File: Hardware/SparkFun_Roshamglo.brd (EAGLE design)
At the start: 35.6 x 72.4 mm, 48 parts, among them IC1 ATTINY84A, J1 R_Ext, J2 USBPCB, Q1 600mA/40V, U1 IR-Receiver, U3 AP2112K-3.3V

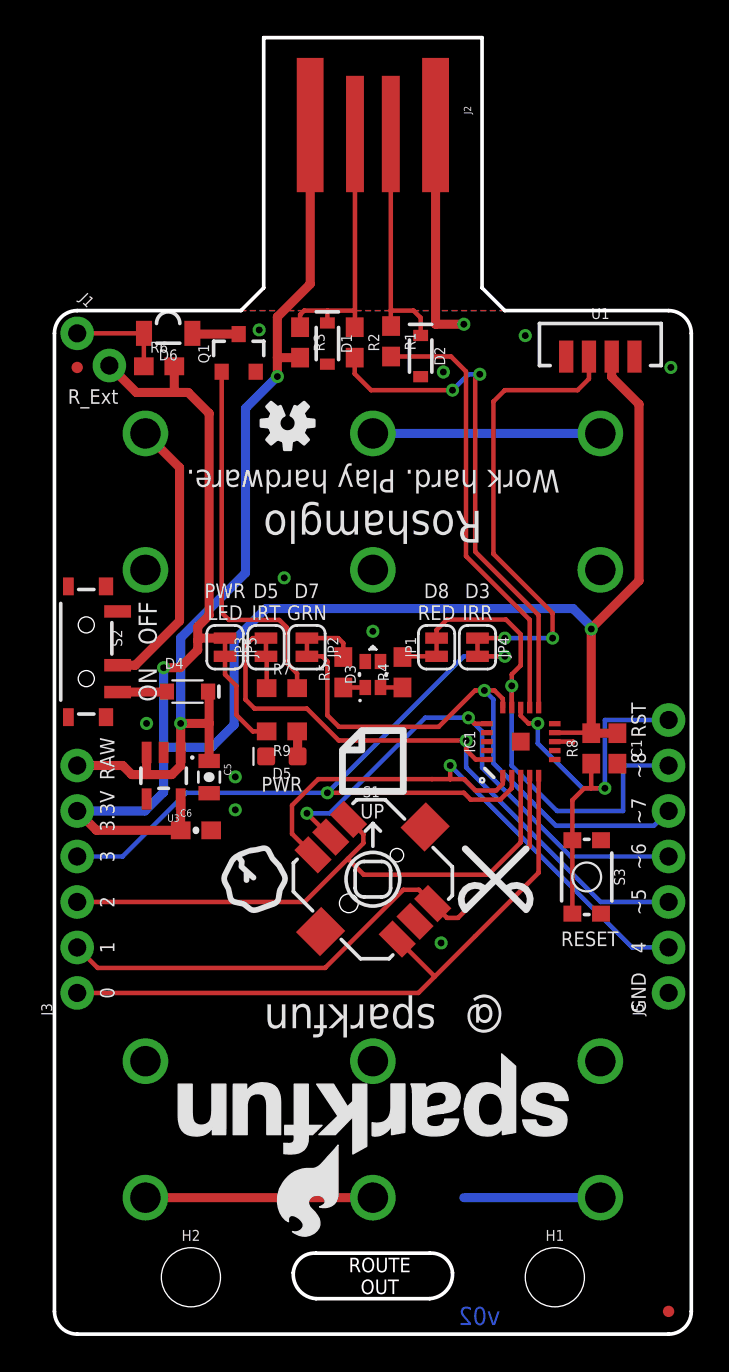
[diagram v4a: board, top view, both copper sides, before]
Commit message: Minor fixes
Added ordering instructions to bottom of board
Removed right angles in traces
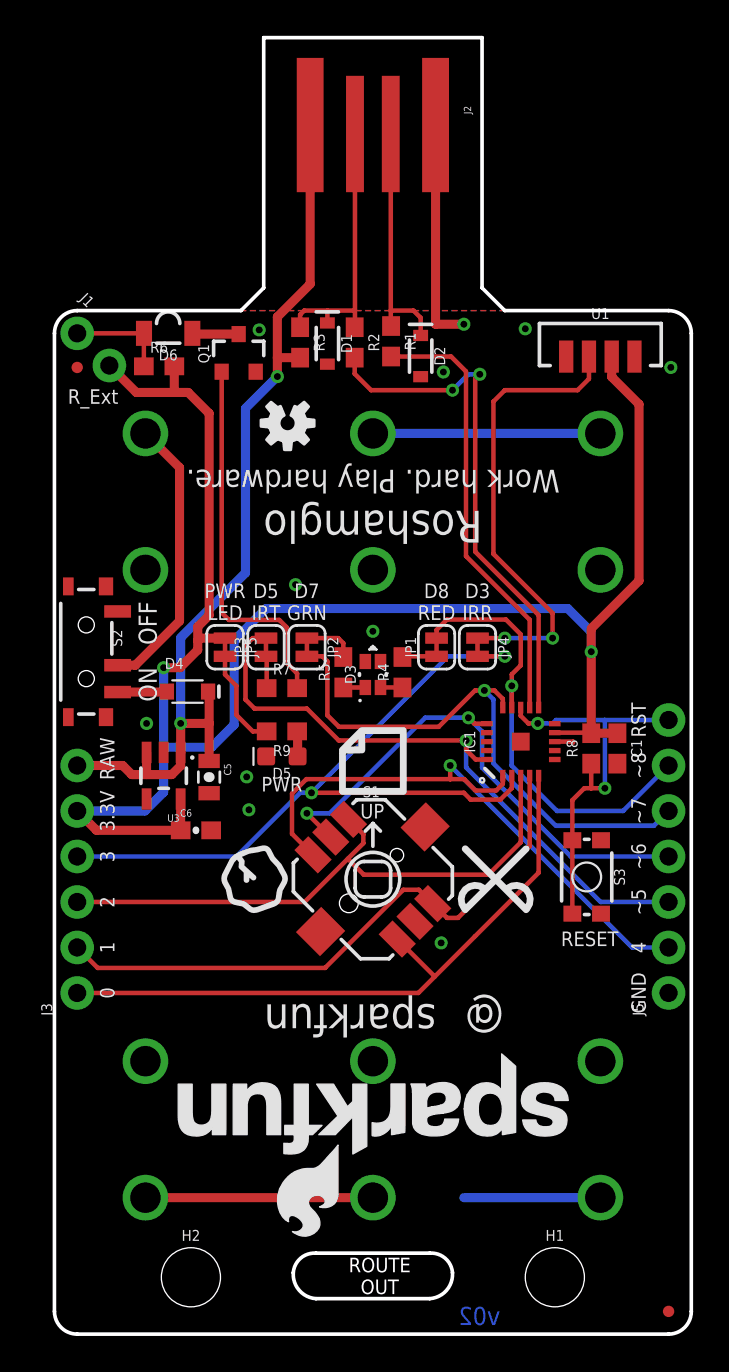
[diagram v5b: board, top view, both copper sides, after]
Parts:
- added U$5: SPECIAL_INSTRUCTIONS-ORDERING, SparkFun-Aesthetics:ORDERING_INSTRUCTIONS
- moved U$4 0.25 mm to (17.8, 67.3)
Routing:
- net !RESET: track 24.7 -> 22.6 mm
- net 8: track 26.8 -> 25.4 mm
- net 3.3V: track 102.5 -> 103.6 mm
- net 3: track 41.4 -> 42.3 mm
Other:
- board text added: "PCB Thickness: 0.078 inch"
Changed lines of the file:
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@@
 <layer number="45" name="Holes" color="7" fill="1" visible="no" active="yes"/>
 <layer number="46" name="Milling" color="3" fill="1" visible="no" active="yes"/>
-<layer number="47" name="Measures" color="7" fill="1" visible="no" active="yes"/>
+<layer number="47" name="Measures" color="7" fill="1" visible="yes" active="yes"/>
 <layer number="51" name="tDocu" color="6" fill="1" visible="yes" active="yes"/>
 <layer number="52" name="bDocu" color="7" fill="1" visible="no" active="yes"/>
@@
 <text x="18.161" y="2.2352" size="0.8128" layer="20" font="vector" ratio="15" align="bottom-center">ROUTE
 OUT</text>
-<text x="17.78" y="55.626" size="1.4224" layer="22" font="vector" ratio="15" rot="SMR180" align="bottom-center">Hack me! sfe.io/roshamglo</text>
+<text x="17.78" y="55.626" size="1.27" layer="22" font="vector" ratio="15" rot="SMR180" align="bottom-center">Hack me! sfe.io/roshamglo</text>
 <text x="17.78" y="48.26" size="1.27" layer="21" font="vector" ratio="15" rot="SR180" align="bottom-center">Work hard. Play hardware.</text>
 <text x="16.51" y="18.415" size="1.778" layer="21" font="vector" ratio="15" rot="SR180" align="bottom-center">sparkfun</text>
-<polygon width="0.0254" layer="22">
-<vertex x="12.1666" y="71.374"/>
-<vertex x="11.7348" y="72.136"/>
-<vertex x="23.8252" y="72.136"/>
-<vertex x="23.3934" y="71.374"/>
-</polygon>
 <wire x1="14.605" y1="4.5212" x2="20.955" y2="4.5212" width="0.2032" layer="20"/>
 <wire x1="20.955" y1="4.5212" x2="22.225" y2="3.429" width="0.2032" layer="20" curve="-90"/>
@@
 LED</text>
 <text x="24.003" y="18.542" size="1.778" layer="21" ratio="30" rot="SR180" align="bottom-center">@</text>
+<text x="-34.29" y="-35.56" size="1.778" layer="51" font="vector" ratio="15" align="center-left">PCB Thickness: 0.078 inch</text>
 </plain>
 <attributes>
@@
 <element name="H1" library="SparkFun-Hardware" package="STAND-OFF" value="STAND-OFF" x="27.94" y="3.175"/>
 <element name="H2" library="SparkFun-Hardware" package="STAND-OFF" value="STAND-OFF" x="7.62" y="3.175"/>
-<element name="U$4" library="Roshamglo" package="ROSHAMGLO_LOGO_0.4" value="" x="17.78" y="67.056" rot="MR180"/>
+<element name="U$4" library="Roshamglo" package="ROSHAMGLO_LOGO_0.4" value="" x="17.78" y="67.31" rot="MR180"/>
 <element name="S3" library="SparkFun-Switches" package="TACTILE_SWITCH_SMD_4.6X2.8MM" value="" x="29.718" y="25.527" rot="R270">
 <attribute name="PROD_ID" value="SWCH-13065" x="29.718" y="25.527" size="1.778" layer="27" font="vector" ratio="15" rot="R270" display="off"/>
@@
 <attribute name="PROD_ID" value="CONN-08437" x="1.27" y="19.05" size="0.8128" layer="27" ratio="30" rot="R90" display="off"/>
 </element>
+<element name="U$5" library="SparkFun-Aesthetics" package="ORDERING_INSTRUCTIONS" value="SPECIAL_INSTRUCTIONS-ORDERING" x="-36.83" y="-21.59"/>
 </elements>
 <signals>
@@
 <wire x1="7.046" y1="29.8784" x2="7.046" y2="28.1339" width="0.508" layer="1"/>
 <wire x1="7.046" y1="28.1339" x2="7.0494" y2="28.1305" width="0.508" layer="1"/>
-<via x="29.972" y="39.37" extent="1-16" drill="0.381"/>
+<via x="29.972" y="38.1" extent="1-16" drill="0.381"/>
 <wire x1="32.639" y1="51.921528125" x2="32.639" y2="42.06523125" width="0.508" layer="1"/>
 <wire x1="31.115" y1="54.58" x2="31.115" y2="53.445528125" width="0.508" layer="1"/>
@@
 <wire x1="29.972" y1="33.5835" x2="29.972" y2="33.5525" width="0.254" layer="1"/>
 <via x="6.096" y="37.211" extent="1-16" drill="0.381"/>
-<wire x1="11.811" y1="40.513" x2="28.956" y2="40.513" width="0.508" layer="16"/>
-<wire x1="28.956" y1="40.513" x2="29.972" y2="39.497" width="0.508" layer="16"/>
-<wire x1="29.972" y1="39.497" x2="29.972" y2="39.37" width="0.508" layer="16"/>
+<wire x1="11.811" y1="40.513" x2="28.66445625" y2="40.513" width="0.508" layer="16"/>
+<wire x1="28.66445625" y1="40.513" x2="29.972" y2="39.20545625" width="0.508" layer="16"/>
+<wire x1="29.972" y1="39.20545625" x2="29.972" y2="38.1" width="0.508" layer="16"/>
 <wire x1="32.639" y1="42.06523125" x2="29.972" y2="39.39823125" width="0.508" layer="1"/>
-<wire x1="29.972" y1="39.39823125" x2="29.972" y2="39.37" width="0.508" layer="1"/>
-<wire x1="29.972" y1="33.5835" x2="29.972" y2="39.37" width="0.508" layer="1"/>
+<wire x1="29.972" y1="39.39823125" x2="29.972" y2="38.1" width="0.508" layer="1"/>
+<wire x1="29.972" y1="33.5835" x2="29.972" y2="38.1" width="0.508" layer="1"/>
 <contactref element="J1" pad="2"/>
 <wire x1="3.06605" y1="54.083946875" x2="4.571996875" y2="52.578" width="0.508" layer="1"/>
@@
 <via x="22.86" y="56.388" extent="1-16" drill="0.381"/>
 <contactref element="Q1" pad="2"/>
-<via x="26.289" y="55.753" extent="1-16" drill="0.381"/>
+<via x="26.289" y="56.134" extent="1-16" drill="0.381"/>
 <via x="34.417" y="53.975" extent="1-16" drill="0.381"/>
-<via x="12.827" y="42.2275" extent="1-16" drill="0.381"/>
+<via x="13.462" y="41.8465" extent="1-16" drill="0.381"/>
 <via x="21.59" y="21.844" extent="1-16" drill="0.381"/>
 <contactref element="J5" pad="1"/>
 <via x="11.43" y="56.0705" extent="1-16" drill="0.381"/>
 <via x="17.78" y="39.243" extent="1-16" drill="0.381"/>
-<via x="10.0965" y="29.2735" extent="1-16" drill="0.381"/>
-<via x="10.0965" y="31.115" extent="1-16" drill="0.381"/>
+<via x="10.8585" y="29.2735" extent="1-16" drill="0.381"/>
+<via x="10.7315" y="31.115" extent="1-16" drill="0.381"/>
 <via x="5.1435" y="34.0995" extent="1-16" drill="0.381"/>
 <wire x1="30.48" y1="7.62" x2="22.86" y2="7.62" width="0.508" layer="16"/>
@@
 <wire x1="30.734" y1="30.48" x2="29.972" y2="30.48" width="0.254" layer="1"/>
 <wire x1="29.972" y1="30.48" x2="29.972" y2="31.8525" width="0.254" layer="1"/>
-<wire x1="26.9875" y1="34.0995" x2="26.9875" y2="32.979190625" width="0.254" layer="16"/>
-<wire x1="26.9875" y1="32.979190625" x2="29.486690625" y2="30.48" width="0.254" layer="16"/>
-<wire x1="29.486690625" y1="30.48" x2="30.734" y2="30.48" width="0.254" layer="16"/>
 <contactref element="S3" pad="1"/>
 <contactref element="S3" pad="2"/>
@@
 <wire x1="30.734" y1="30.48" x2="30.734" y2="34.29" width="0.254" layer="16"/>
 <wire x1="30.734" y1="34.29" x2="34.29" y2="34.29" width="0.254" layer="16"/>
+<wire x1="26.9875" y1="34.0995" x2="27.813" y2="34.0995" width="0.254" layer="16"/>
+<wire x1="27.813" y1="34.0995" x2="28.0035" y2="34.29" width="0.254" layer="16"/>
+<wire x1="28.0035" y1="34.29" x2="30.734" y2="34.29" width="0.254" layer="16"/>
 </signal>
 <signal name="8">
@@
 <wire x1="25.527" y1="36.187" x2="25.535" y2="36.195" width="0.254" layer="16"/>
 <contactref element="J5" pad="6"/>
-<wire x1="34.29" y1="31.75" x2="31.75" y2="31.75" width="0.254" layer="16"/>
-<wire x1="31.75" y1="31.75" x2="31.75" y2="29.21" width="0.254" layer="16"/>
 <wire x1="31.75" y1="29.21" x2="28.067" y2="29.21" width="0.254" layer="16"/>
+<wire x1="34.29" y1="31.75" x2="31.75" y2="29.21" width="0.254" layer="16"/>
 </signal>
 <signal name="9">
@@
 <contactref element="IC1" pad="1"/>
 <contactref element="S1" pad="C"/>
-<wire x1="14.726409375" y1="30.988" x2="13.26406875" y2="29.525659375" width="0.254" layer="1"/>
-<wire x1="13.26406875" y1="29.525659375" x2="13.26406875" y2="27.936028125" width="0.254" layer="1"/>
+<wire x1="13.26406875" y1="27.936028125" x2="13.26406875" y2="30.185815625" width="0.254" layer="1"/>
+<wire x1="13.26406875" y1="30.185815625" x2="14.066253125" y2="30.988" width="0.254" layer="1"/>
+<wire x1="14.066253125" y1="30.988" x2="22.098" y2="30.988" width="0.254" layer="1"/>
 <wire x1="13.26406875" y1="27.936028125" x2="14.43891875" y2="26.761178125" width="0.254" layer="1"/>
-<wire x1="14.726409375" y1="30.988" x2="21.082" y2="30.988" width="0.254" layer="1"/>
 <wire x1="22.098" y1="30.988" x2="22.88060625" y2="30.988" width="0.254" layer="1"/>
 <wire x1="22.88060625" y1="30.988" x2="23.51560625" y2="30.353" width="0.254" layer="1"/>
@@
 <via x="22.098" y="31.75" extent="1-16" drill="0.381"/>
 <wire x1="22.098" y1="31.75" x2="22.098" y2="30.988" width="0.254" layer="1"/>
-<wire x1="22.098" y1="30.988" x2="21.082" y2="30.988" width="0.254" layer="1"/>
 </signal>
 <signal name="3">
 <contactref element="IC1" pad="2"/>
 <contactref element="JP4" pad="2"/>
-<wire x1="7.366" y1="30.226" x2="15.24" y2="30.226" width="0.254" layer="16"/>
-<via x="15.24" y="30.226" extent="1-16" drill="0.381"/>
+<wire x1="13.716" y1="30.226" x2="14.351" y2="30.226" width="0.254" layer="16"/>
+<via x="14.351" y="30.226" extent="1-16" drill="0.381"/>
 <wire x1="23.622" y1="37.846" x2="25.146" y2="37.846" width="0.254" layer="1"/>
 <via x="25.146" y="37.846" extent="1-16" drill="0.381"/>
@@
 <wire x1="24.89516875" y1="29.845" x2="23.241" y2="29.845" width="0.254" layer="1"/>
 <wire x1="23.241" y1="29.845" x2="22.86" y2="30.226" width="0.254" layer="1"/>
-<wire x1="22.86" y1="30.226" x2="15.24" y2="30.226" width="0.254" layer="1"/>
-<wire x1="25.146" y1="37.846" x2="22.86" y2="37.846" width="0.254" layer="16"/>
-<wire x1="22.86" y1="37.846" x2="15.24" y2="30.226" width="0.254" layer="16"/>
+<wire x1="22.86" y1="30.226" x2="14.351" y2="30.226" width="0.254" layer="1"/>
+<wire x1="25.146" y1="37.846" x2="21.971" y2="37.846" width="0.254" layer="16"/>
 <contactref element="J3" pad="4"/>
-<wire x1="7.366" y1="30.226" x2="3.81" y2="26.67" width="0.254" layer="16"/>
-<wire x1="3.81" y1="26.67" x2="1.27" y2="26.67" width="0.254" layer="16"/>
+<wire x1="13.716" y1="30.226" x2="10.16" y2="26.67" width="0.254" layer="16"/>
+<wire x1="10.16" y1="26.67" x2="1.27" y2="26.67" width="0.254" layer="16"/>
+<wire x1="21.971" y1="37.846" x2="14.351" y2="30.226" width="0.254" layer="16"/>
 </signal>
 <signal name="2">
